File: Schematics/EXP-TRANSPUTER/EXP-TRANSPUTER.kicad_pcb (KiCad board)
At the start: 4 copper layers, 170 x 59 mm, 36 parts, among them IC2 74HCT373DW, IC5 CY62256N, J1 DIN41612_03x32_ABC_Male_Hor, J10 Conn_02x02_Odd_Even, J3 Conn_01x08, J4 Conn_01x08, J5 Conn_01x08, J6 Conn_01x08, J7 Conn_02x02_Odd_Even, J8 Conn_02x02_Odd_Even, J9 Conn_02x02_Odd_Even, U11 IMSC011, U2 ATF1502AS, U7 SN74LVC245APW

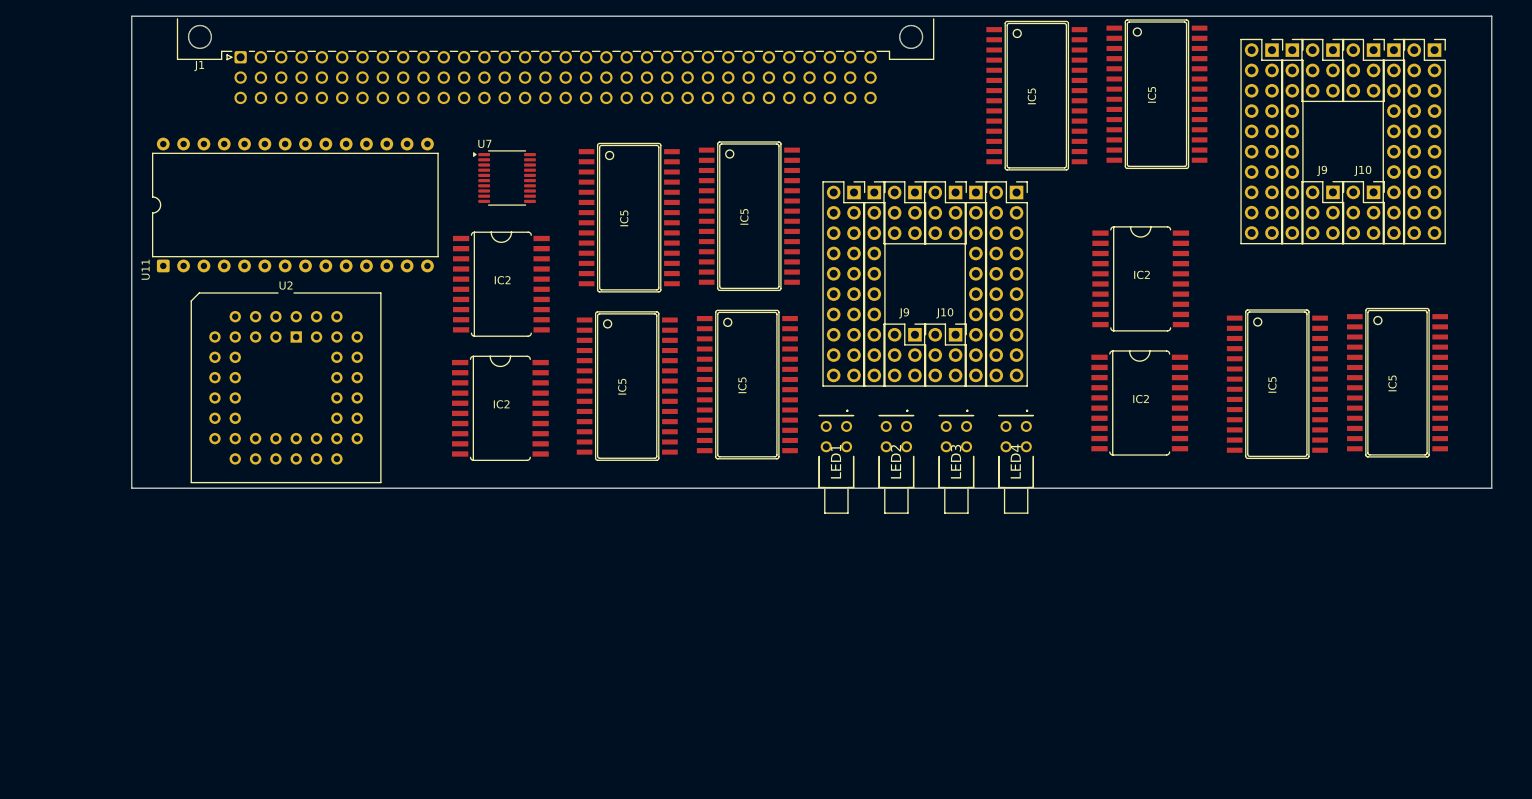
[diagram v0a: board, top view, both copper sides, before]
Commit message: EXP card, updated PCB dimensions
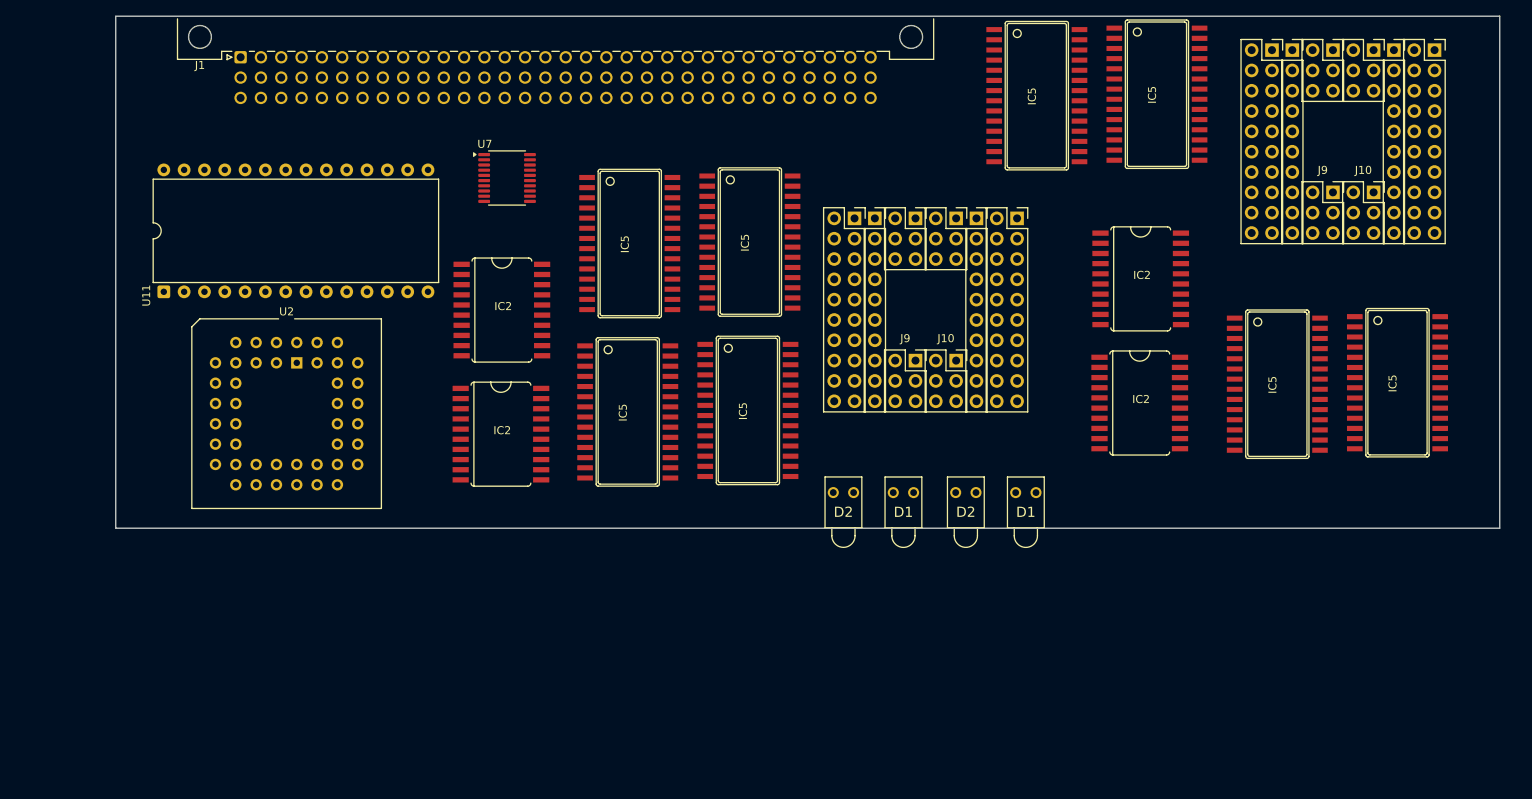
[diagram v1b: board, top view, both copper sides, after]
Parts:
- removed LED1, LED2, LED3, LED4: LTL-42D1NMHDP1, LTL-42D1NMHDP1:LTL42D1NMHDP1
- added D1: LED, LTL-4221NHBP:LTL4221NHBP, F.Cu at (180.5, 100.6)
- added D1: LED, LTL-4221NHBP:LTL4221NHBP, F.Cu at (165.2, 100.6)
- added D2: LED, LTL-4221NHBP:LTL4221NHBP, F.Cu at (173.0, 100.5)
- added D2: LED, LTL-4221NHBP:LTL4221NHBP, F.Cu at (157.7, 100.5)
- moved IC5 3.23 mm to (132.3, 69.4)
- moved IC5 3.23 mm to (147.0, 90.3)
- moved IC5 3.23 mm to (147.3, 69.2)
- moved IC5 3.23 mm to (132.0, 90.5)
- moved J10 3.23 mm to (173.0, 84.1)
- moved IC2 3.23 mm to (116.3, 77.7)
- moved IC2 3.23 mm to (116.1, 93.2)
- moved J9 3.23 mm to (168.0, 84.1)
- moved U11 3.23 mm to (74.0, 75.5)
- moved U2 3.23 mm to (90.6, 84.3)
- moved J3 3.23 mm to (160.3, 66.3)
- moved J4 3.23 mm to (180.7, 66.3)
- moved J5 3.23 mm to (162.9, 66.3)
- moved J8 3.23 mm to (173.0, 66.3)
- moved J6 3.23 mm to (175.6, 66.3)
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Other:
- board size 170 x 59 mm -> 173 x 64 mm

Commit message: EXP Card, change to dimensions
Brought dimensions in a little to ensure it fits within case.
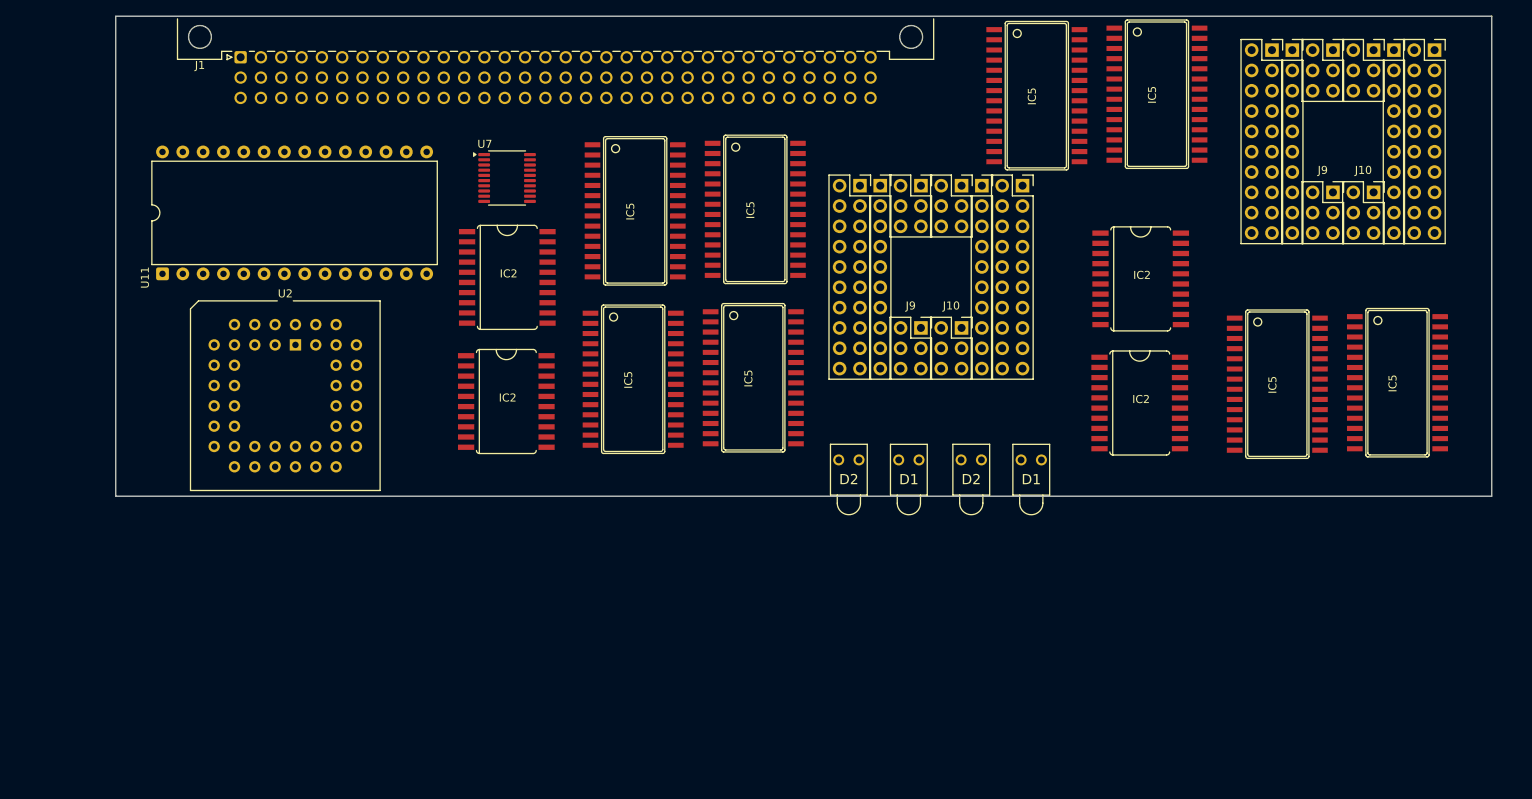
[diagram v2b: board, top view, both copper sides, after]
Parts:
- moved D1 4.14 mm to (181.2, 96.5)
- moved D1 4.14 mm to (165.9, 96.5)
- moved D2 4.14 mm to (173.7, 96.5)
- moved D2 4.14 mm to (158.4, 96.5)
- moved IC2 4.14 mm to (116.9, 73.6)
- moved IC2 4.14 mm to (116.8, 89.2)
- moved IC5 4.14 mm to (132.9, 65.3)
- moved IC5 4.14 mm to (147.7, 86.2)
- moved IC5 4.14 mm to (147.9, 65.1)
- moved IC5 4.14 mm to (132.7, 86.4)
- moved J10 4.14 mm to (173.7, 80.0)
- moved J9 4.14 mm to (168.6, 80.0)
- moved J3 4.14 mm to (161.0, 62.2)
- moved J4 4.14 mm to (181.3, 62.2)
- moved J5 4.14 mm to (163.6, 62.2)
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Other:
- board size 173 x 64 mm -> 172 x 60 mm
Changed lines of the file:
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@@
 	(footprint "SO20W"
 		(layer "F.Cu")
-		(at 116.268146 77.731717 -90)
+		(at 116.945594 73.647109 -90)
 		(descr "Wide Small Outline package 300 mil")
 		(property "Reference" "IC2"
@@
 	(footprint "Connector_PinSocket_2.54mm:PinSocket_1x10_P2.54mm_Vertical"
 		(layer "F.Cu")
-		(at 162.888146 66.271717)
+		(at 163.565594 62.187109)
 		(descr "Through hole straight socket strip, 1x10, 2.54mm pitch, single row (from Kicad 4.0.7), script generated")
 		(tags "Through hole socket strip THT 1x10 2.54mm single row")
@@
 	(footprint "SOP28N"
 		(layer "F.Cu")
-		(at 132.252146 69.416717 -90)
+		(at 132.929594 65.332109 -90)
 		(property "Reference" "IC5"
 			(at 1.2065 0 90)
@@
 	(footprint "Connector_PinSocket_2.54mm:PinSocket_2x10_P2.54mm_Vertical"
 		(layer "F.Cu")
-		(at 160.348146 66.271717)
+		(at 161.025594 62.187109)
 		(descr "Through hole straight socket strip, 2x10, 2.54mm pitch, double cols (from Kicad 4.0.7), script generated")
 		(tags "Through hole socket strip THT 2x10 2.54mm double row")
@@
 	(footprint "Connector_PinSocket_2.54mm:PinSocket_2x03_P2.54mm_Vertical"
 		(layer "F.Cu")
-		(at 167.968146 66.271717)
+		(at 168.645594 62.187109)
 		(descr "Through hole straight socket strip, 2x03, 2.54mm pitch, double cols (from Kicad 4.0.7), script generated")
 		(tags "Through hole socket strip THT 2x03 2.54mm double row")
@@
 	(footprint "LTL-4221NHBP:LTL4221NHBP"
 		(layer "F.Cu")
-		(at 172.992115 100.545592)
+		(at 173.669563 96.460984)
 		(descr "LTL-4221NHBP-2")
 		(tags "LED")
@@
 	(footprint "LTL-4221NHBP:LTL4221NHBP"
 		(layer "F.Cu")
-		(at 180.492115 100.55082)
+		(at 181.169563 96.466212)
 		(descr "LTL-4221NHBP-2")
 		(tags "LED")
@@
 	(footprint "Connector_PinSocket_2.54mm:PinSocket_1x10_P2.54mm_Vertical"
 		(layer "F.Cu")
-		(at 175.588146 66.271717)
+		(at 176.265594 62.187109)
 		(descr "Through hole straight socket strip, 1x10, 2.54mm pitch, single row (from Kicad 4.0.7), script generated")
 		(tags "Through hole socket strip THT 1x10 2.54mm single row")
@@
 	(footprint "Connector_PinSocket_2.54mm:PinSocket_2x03_P2.54mm_Vertical"
 		(layer "F.Cu")
-		(at 173.048146 66.271717)
+		(at 173.725594 62.187109)
 		(descr "Through hole straight socket strip, 2x03, 2.54mm pitch, double cols (from Kicad 4.0.7), script generated")
 		(tags "Through hole socket strip THT 2x03 2.54mm double row")
@@
 	(footprint "LTL-4221NHBP:LTL4221NHBP"
 		(layer "F.Cu")
-		(at 157.692115 100.545592)
+		(at 158.369563 96.460984)
 		(descr "LTL-4221NHBP-2")
 		(tags "LED")
@@
 	(footprint "SO20W"
 		(layer "F.Cu")
-		(at 116.147346 93.246717 -90)
+		(at 116.824794 89.162109 -90)
 		(descr "Wide Small Outline package 300 mil")
 		(property "Reference" "IC2"
@@
 	(footprint "SOP28N"
 		(layer "F.Cu")
-		(at 147.018146 90.281717 -90)
+		(at 147.695594 86.197109 -90)
 		(property "Reference" "IC5"
 			(at 1.2065 0 90)
@@
 	(footprint "Package_LCC:PLCC-44_THT-Socket"
 		(layer "F.Cu")
-		(at 90.628146 84.331717)
+		(at 90.463421 82.086002)
 		(descr "PLCC, 44 pins, through hole")
 		(tags "plcc leaded")
@@
 	(footprint "LTL-4221NHBP:LTL4221NHBP"
 		(layer "F.Cu")
-		(at 165.192115 100.55082)
+		(at 165.869563 96.466212)
 		(descr "LTL-4221NHBP-2")
 		(tags "LED")
@@
 	(footprint "Connector_PinSocket_2.54mm:PinSocket_2x03_P2.54mm_Vertical"
 		(layer "F.Cu")
-		(at 173.048146 84.051717)
+		(at 173.725594 79.967109)
 		(descr "Through hole straight socket strip, 2x03, 2.54mm pitch, double cols (from Kicad 4.0.7), script generated")
 		(tags "Through hole socket strip THT 2x03 2.54mm double row")
@@
 	(footprint "Connector_PinSocket_2.54mm:PinSocket_2x10_P2.54mm_Vertical"
 		(layer "F.Cu")
-		(at 180.668146 66.271717)
+		(at 181.345594 62.187109)
 		(descr "Through hole straight socket strip, 2x10, 2.54mm pitch, double cols (from Kicad 4.0.7), script generated")
 		(tags "Through hole socket strip THT 2x10 2.54mm double row")
@@
 	(footprint "Package_DIP:DIP-28_W15.24mm"
 		(layer "F.Cu")
-		(at 74.008146 75.451717 90)
+		(at 73.843421 73.206002 90)
 		(descr "28-lead though-hole mounted DIP package, row spacing 15.24mm (600 mils)")
 		(tags "THT DIP DIL PDIP 2.54mm 15.24mm 600mil")
@@
 	(footprint "SOP28N"
 		(layer "F.Cu")
-		(at 147.268146 69.231717 -90)
+		(at 147.945594 65.147109 -90)
 		(property "Reference" "IC5"
 			(at 1.2065 0 90)
@@
 	(footprint "SOP28N"
 		(layer "F.Cu")
-		(at 132.002146 90.466717 -90)
+		(at 132.679594 86.382109 -90)
 		(property "Reference" "IC5"
 			(at 1.2065 0 90)
@@
 	(footprint "Connector_PinSocket_2.54mm:PinSocket_2x03_P2.54mm_Vertical"
 		(layer "F.Cu")
-		(at 167.968146 84.051717)
+		(at 168.645594 79.967109)
 		(descr "Through hole straight socket strip, 2x03, 2.54mm pitch, double cols (from Kicad 4.0.7), script generated")
 		(tags "Through hole socket strip THT 2x03 2.54mm double row")
@@
 	(gr_rect
 		(start 68 41)
-		(end 241 105)
+		(end 240 101)
 		(stroke
 			(width 0.05)
@@
 	(dimension
 		(type orthogonal)
+		(layer "Dwgs.User")
+		(pts
+			(xy 240 41) (xy 240 101)
+		)
+		(height 9)
+		(orientation 1)
+		(format
+			(prefix "")
+			(suffix "")
+			(units 3)
+			(units_format 0)
+			(precision 4)
+			(suppress_zeroes yes)
+		)
+		(style
+			(thickness 0.1)
+			(arrow_length 1.27)
+			(text_position_mode 0)
+			(arrow_direction outward)
+			(extension_height 0.58642)
+			(extension_offset 0.5)
+			(keep_text_aligned yes)
+		)
+		(gr_text "60"
+			(at 247.85 71 90)
+			(layer "Dwgs.User")
+			(effects
+				(font
+					(size 1 1)
+					(thickness 0.15)
+				)
+			)
+		)
+	)
+	(dimension
+		(type orthogonal)
+		(layer "Dwgs.User")
+		(pts
+			(xy 240 101) (xy 68 101)
+		)
+		(height 9)
+		(orientation 0)
+		(format
+			(prefix "")
+			(suffix "")
+			(units 3)
+			(units_format 0)
+			(precision 4)
+			(suppress_zeroes yes)
+		)
+		(style
+			(thickness 0.1)
+			(arrow_length 1.27)
+			(text_position_mode 0)
+			(arrow_direction outward)
+			(extension_height 0.58642)
+			(extension_offset 0.5)
+			(keep_text_aligned yes)
+		)
+		(gr_text "172"
+			(at 154 108.85 0)
+			(layer "Dwgs.User")
+			(effects
+				(font
+					(size 1 1)
+					(thickness 0.15)
+				)
+			)
+		)
+	)
+	(dimension
+		(type orthogonal)
 		(layer "Edge.Cuts")
 		(pts
-			(xy 70 41) (xy 75.45 41.2)
+			(xy 68 41.2) (xy 75.45 41.2)
 		)
 		(height -2.15)
@@
 			(keep_text_aligned yes)
 		)
-		(gr_text "5.45"
-			(at 72.725 37.7 0)
+		(gr_text "7.45"
+			(at 71.725 37.9 0)
 			(layer "Edge.Cuts")
 			(effects

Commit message: Case tweaks, rexport
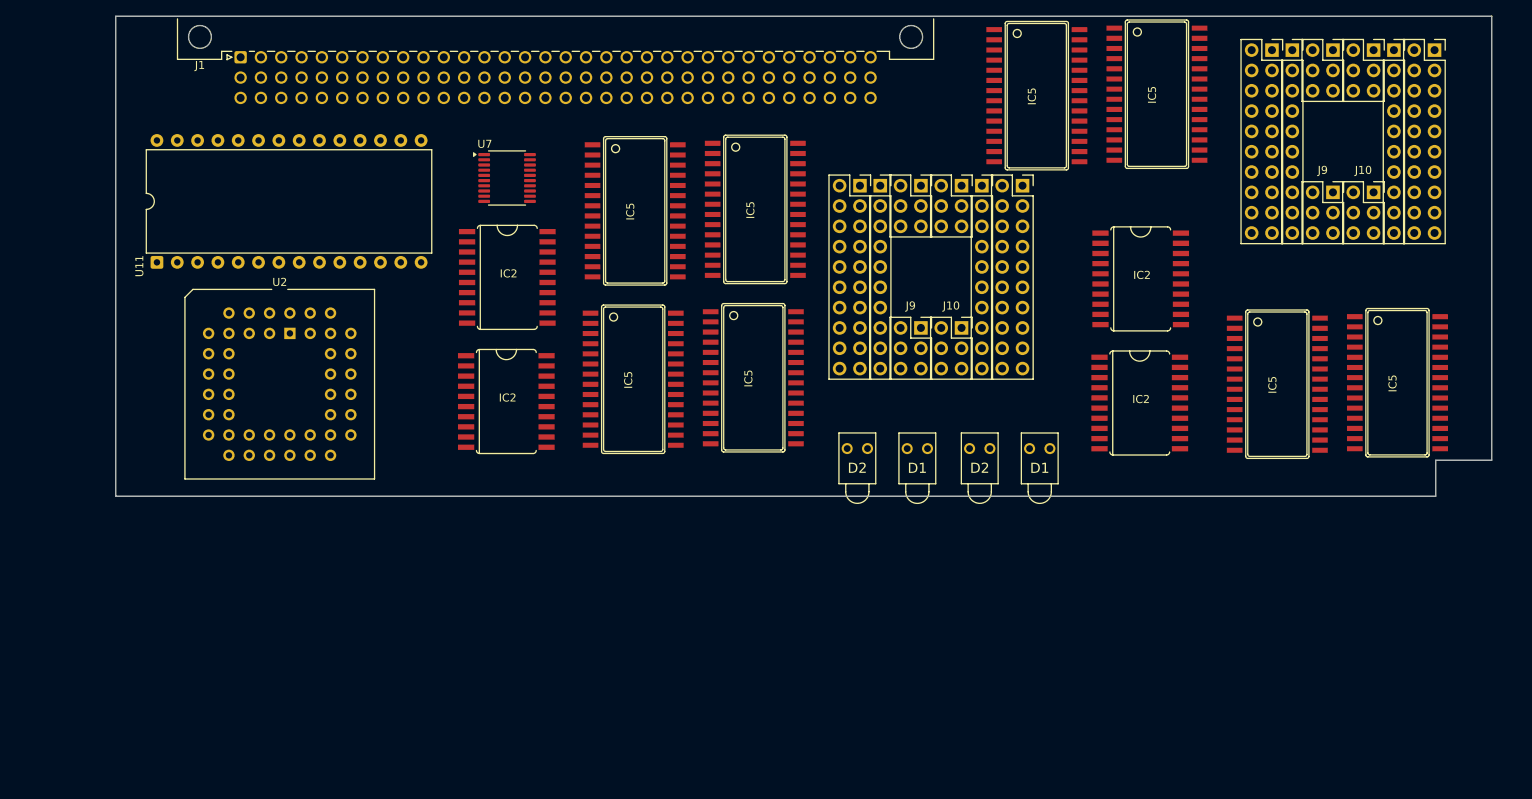
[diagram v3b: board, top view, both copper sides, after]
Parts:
- moved D1 1.77 mm to (166.9, 95.0)
- moved D2 1.77 mm to (159.4, 95.0)
- moved D1 1.77 mm to (182.2, 95.0)
- moved D2 1.77 mm to (174.7, 95.0)
- moved U11 1.59 mm to (73.2, 71.8)
- moved U2 1.59 mm to (89.8, 80.7)
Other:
- outline, holes or cut-outs redrawn
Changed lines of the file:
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@@
 			(psa4output no)
 			(plot_black_and_white yes)
+			(plotinvisibletext no)
 			(sketchpadsonfab no)
 			(plotpadnumbers no)
@@
 	(footprint "LTL-4221NHBP:LTL4221NHBP"
 		(layer "F.Cu")
-		(at 173.669563 96.460984)
+		(at 174.73 95.044772)
 		(descr "LTL-4221NHBP-2")
 		(tags "LED")
@@
 	(footprint "LTL-4221NHBP:LTL4221NHBP"
 		(layer "F.Cu")
-		(at 181.169563 96.466212)
+		(at 182.23 95.05)
 		(descr "LTL-4221NHBP-2")
 		(tags "LED")
@@
 	(footprint "LTL-4221NHBP:LTL4221NHBP"
 		(layer "F.Cu")
-		(at 158.369563 96.460984)
+		(at 159.43 95.044772)
 		(descr "LTL-4221NHBP-2")
 		(tags "LED")
@@
 	(footprint "Package_LCC:PLCC-44_THT-Socket"
 		(layer "F.Cu")
-		(at 90.463421 82.086002)
+		(at 89.77 80.65)
 		(descr "PLCC, 44 pins, through hole")
 		(tags "plcc leaded")
@@
 	(footprint "LTL-4221NHBP:LTL4221NHBP"
 		(layer "F.Cu")
-		(at 165.869563 96.466212)
+		(at 166.93 95.05)
 		(descr "LTL-4221NHBP-2")
 		(tags "LED")
@@
 	(footprint "Package_DIP:DIP-28_W15.24mm"
 		(layer "F.Cu")
-		(at 73.843421 73.206002 90)
+		(at 73.15 71.77 90)
 		(descr "28-lead though-hole mounted DIP package, row spacing 15.24mm (600 mils)")
 		(tags "THT DIP DIL PDIP 2.54mm 15.24mm 600mil")
@@
 		)
 	)
-	(gr_rect
+	(gr_line
 		(start 68 41)
-		(end 240 101)
+		(end 68 101)
+		(stroke
+			(width 0.05)
+			(type default)
+		)
+		(layer "Edge.Cuts")
+	)
+	(gr_line
+		(start 68 101)
+		(end 233 101)
+		(stroke
+			(width 0.05)
+			(type default)
+		)
+		(layer "Edge.Cuts")
+	)
+	(gr_line
+		(start 240 96.5)
+		(end 240 41)
+		(stroke
+			(width 0.05)
+			(type default)
+		)
+		(layer "Edge.Cuts")
+	)
+	(gr_line
+		(start 240 96.5)
+		(end 233 96.5)
+		(stroke
+			(width 0.05)
+			(type default)
+		)
+		(layer "Edge.Cuts")
+	)
+	(gr_line
+		(start 240 41)
+		(end 68 41)
+		(stroke
+			(width 0.05)
+			(type default)
+		)
+		(layer "Edge.Cuts")
+	)
+	(gr_line
+		(start 233 101)
+		(end 233 96.5)
 		(stroke
 			(width 0.05)
 			(type default)
 		)
-		(fill no)
 		(layer "Edge.Cuts")
 	)
@@
 			(layer "Dwgs.User")
 			(effects
+				(font
+					(size 1 1)
+					(thickness 0.15)
+				)
+			)
+		)
+	)
+	(dimension
+		(type orthogonal)
+		(layer "Dwgs.User")
+		(pts
+			(xy 240 101) (xy 233 101)
+		)
+		(height 4.5)
+		(orientation 0)
+		(format
+			(prefix "")
+			(suffix "")
+			(units 3)
+			(units_format 0)
+			(precision 4)
+			(suppress_zeroes yes)
+		)
+		(style
+			(thickness 0.1)
+			(arrow_length 1.27)
+			(text_position_mode 0)
+			(arrow_direction outward)
+			(extension_height 0.58642)
+			(extension_offset 0.5)
+			(keep_text_aligned yes)
+		)
+		(gr_text "7"
+			(at 236.5 104.35 0)
+			(layer "Dwgs.User")
+			(effects
+				(font
+					(size 1 1)
+					(thickness 0.15)
+				)
+			)
+		)
+	)
+	(dimension
+		(type orthogonal)
+		(layer "Dwgs.User")
+		(pts
+			(xy 240 101) (xy 240 96.5)
+		)
+		(height 4.5)
+		(orientation 1)
+		(format
+			(prefix "")
+			(suffix "")
+			(units 3)
+			(units_format 0)
+			(precision 4)
+			(suppress_zeroes yes)
+		)
+		(style
+			(thickness 0.1)
+			(arrow_length 1.27)
+			(text_position_mode 0)
+			(arrow_direction outward)
+			(extension_height 0.58642)
+			(extension_offset 0.5)
+			(keep_text_aligned yes)
+		)
+		(gr_text "4.5"
+			(at 243.35 98.75 90)
+			(layer "Dwgs.User")
+			(effects
